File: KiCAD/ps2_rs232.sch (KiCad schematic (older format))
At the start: 10 parts, among them P2 keyboard, P3 ICSP, U6 PIC12F1572

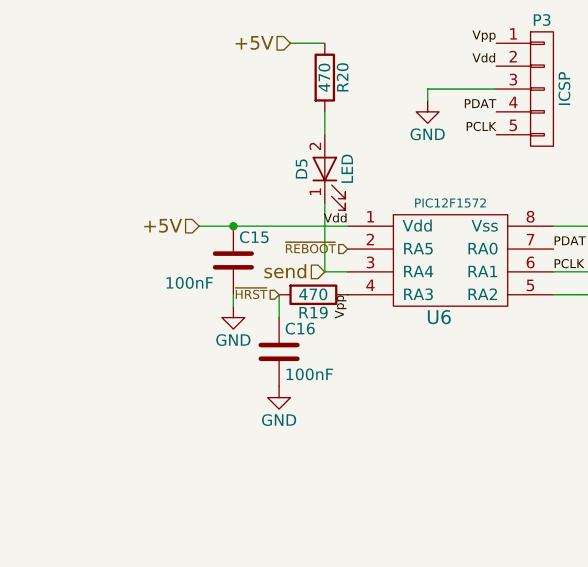
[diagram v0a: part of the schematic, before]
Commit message: ajout code SDCard
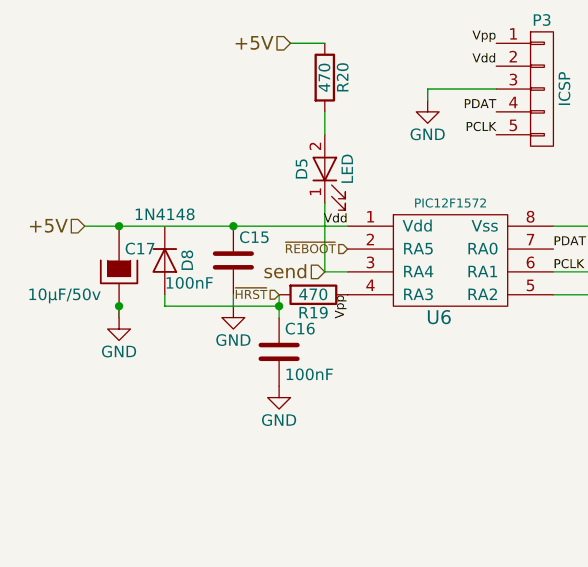
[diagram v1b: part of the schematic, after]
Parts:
- added C17: 10µF/50v, symbol CP-RESCUE-forthEx
- added D8: 1N4148, symbol D
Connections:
- wire segments 15 -> 18
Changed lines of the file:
@@
 $EndComp
 $Comp
-L GND #PWR36
+L GND #PWR37
 U 1 1 5872D9BC
 P 7000 4250
-F 0 "#PWR36" H 7000 4000 50  0001 C CNN
+F 0 "#PWR37" H 7000 4000 50  0001 C CNN
 F 1 "GND" H 7000 4100 50  0000 C CNN
 F 2 "" H 7000 4250 50  0000 C CNN
@@
 $EndComp
 $Comp
-L GND #PWR35
+L GND #PWR36
 U 1 1 5872D9D4
 P 6600 4050
-F 0 "#PWR35" H 6600 3800 50  0001 C CNN
+F 0 "#PWR36" H 6600 3800 50  0001 C CNN
 F 1 "GND" H 6600 3900 50  0000 C CNN
 F 2 "" H 6600 4050 50  0000 C CNN
@@
 $EndComp
 $Comp
-L GND #PWR34
+L GND #PWR35
 U 1 1 5872D9E5
 P 5900 3650
-F 0 "#PWR34" H 5900 3400 50  0001 C CNN
+F 0 "#PWR35" H 5900 3400 50  0001 C CNN
 F 1 "GND" H 5900 3500 50  0000 C CNN
 F 2 "" H 5900 3650 50  0000 C CNN
@@
 $EndComp
 Wire Wire Line
-	4050 3650 4700 3650
+	3550 3650 4700 3650
 Connection ~ 4200 3650
 $Comp
-L GND #PWR31
+L GND #PWR32
 U 1 1 5872DA37
 P 4200 4000
-F 0 "#PWR31" H 4200 3750 50  0001 C CNN
+F 0 "#PWR32" H 4200 3750 50  0001 C CNN
 F 1 "GND" H 4200 3850 50  0000 C CNN
 F 2 "" H 4200 4000 50  0000 C CNN
@@
 Text HLabel 6600 3750 0    59   Input ~ 0
 +5V
-Text HLabel 4050 3650 0    59   Input ~ 0
+Text HLabel 3550 3650 0    59   Input ~ 0
 +5V
 Text HLabel 4600 3850 0    59   Input ~ 0
@@
 	4400 3950 4400 4050
 $Comp
-L GND #PWR32
+L GND #PWR33
 U 1 1 5873E590
 P 4400 4350
-F 0 "#PWR32" H 4400 4100 50  0001 C CNN
+F 0 "#PWR33" H 4400 4100 50  0001 C CNN
 F 1 "GND" H 4400 4200 50  0000 C CNN
 F 2 "" H 4400 4350 50  0000 C CNN
@@
 Vdd
 $Comp
-L GND #PWR33
+L GND #PWR34
 U 1 1 5874053C
 P 5050 3100
-F 0 "#PWR33" H 5050 2850 50  0001 C CNN
+F 0 "#PWR34" H 5050 2850 50  0001 C CNN
 F 1 "GND" H 5050 2950 50  0000 C CNN
 F 2 "" H 5050 3100 50  0000 C CNN
@@
 Text HLabel 4400 3950 0    39   Input ~ 0
 ~HRST
+$Comp
+L CP-RESCUE-forthEx C17
+U 1 1 587516E6
+P 3700 3850
+F 0 "C17" H 3725 3950 50  0000 L CNN
+F 1 "10µF/50v" H 3300 3750 50  0000 L CNN
+F 2 "" H 3738 3700 50  0000 C CNN
+F 3 "" H 3700 3850 50  0000 C CNN
+	1    3700 3850
+	1    0    0    -1
+$EndComp
+Connection ~ 3700 3650
+$Comp
+L GND #PWR31
+U 1 1 58751800
+P 3700 4050
+F 0 "#PWR31" H 3700 3800 50  0001 C CNN
+F 1 "GND" H 3700 3900 50  0000 C CNN
+F 2 "" H 3700 4050 50  0000 C CNN
+F 3 "" H 3700 4050 50  0000 C CNN
+	1    3700 4050
+	1    0    0    -1
+$EndComp
+Wire Wire Line
+	3700 4000 3700 4050
+$Comp
+L D D8
+U 1 1 587CEA41
+P 3900 3800
+F 0 "D8" H 3900 3900 50  0000 C CNN
+F 1 "1N4148" V 3700 3800 50  0000 C CNN
+F 2 "" H 3900 3800 50  0000 C CNN
+F 3 "" H 3900 3800 50  0000 C CNN
+	1    3900 3800
+	0    1    1    0
+$EndComp
+Connection ~ 3700 4000
+Wire Wire Line
+	4400 4000 3900 4000
+Wire Wire Line
+	3900 4000 3900 3950
+Connection ~ 4400 4000
 $EndSCHEMATC

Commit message: Ajout des mots CHARS, CHAR+ et CHAR  [CHAR] ['] Modification du mot WORDS: affiche le nombre de mots trouvés dans le dictionnaire EXIT est maintenant visible. >> à faire:      corrigé TONE      ajouter FM/MOD SM/REM      relire 6.1.1900 concernant MOVE, CMOVE et CMOVE>
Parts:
- added R26: 470, symbol R
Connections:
- wire segments 18 -> 19
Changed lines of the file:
@@
 P 5900 3650
 F 0 "#PWR35" H 5900 3400 50  0001 C CNN
-F 1 "GND" H 5900 3500 50  0000 C CNN
+F 1 "GND" H 6000 3600 50  0000 C CNN
 F 2 "" H 5900 3650 50  0000 C CNN
 F 3 "" H 5900 3650 50  0000 C CNN
@@
 Text HLabel 4600 3850 0    59   Input ~ 0
 send
-Wire Wire Line
-	5600 3850 6600 3850
 Wire Wire Line
 	5600 3950 6600 3950
@@
 Text HLabel 4700 3750 0    39   Input ~ 0
 ~REBOOT
+$Comp
+L R R26
+U 1 1 58B73AA2
+P 5900 3850
+F 0 "R26" V 5980 3850 50  0000 C CNN
+F 1 "470" V 5900 3850 50  0000 C CNN
+F 2 "" V 5830 3850 50  0000 C CNN
+F 3 "" H 5900 3850 50  0000 C CNN
+	1    5900 3850
+	0    1    1    0
+$EndComp
+Wire Wire Line
+	6050 3850 6600 3850
+Wire Wire Line
+	5750 3850 5600 3850
 $EndSCHEMATC

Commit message: include la carte SD dans les périphérique boot. ajout des mots ?SDCOK, IMG>SDC et SDC>IMG, NSECTOR dans sdcard.s modfications dans store.s
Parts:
- P2: symbol USB_A -> USB_A-RESCUE-forthEx
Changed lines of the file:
@@
 $EndDescr
 $Comp
-L USB_A P2
+L USB_A-RESCUE-forthEx P2
 U 1 1 5872D906
 P 6900 3950
